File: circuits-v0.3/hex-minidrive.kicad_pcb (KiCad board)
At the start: 4 copper layers, 18 x 48 mm, 81 parts, among them X1 16MHz

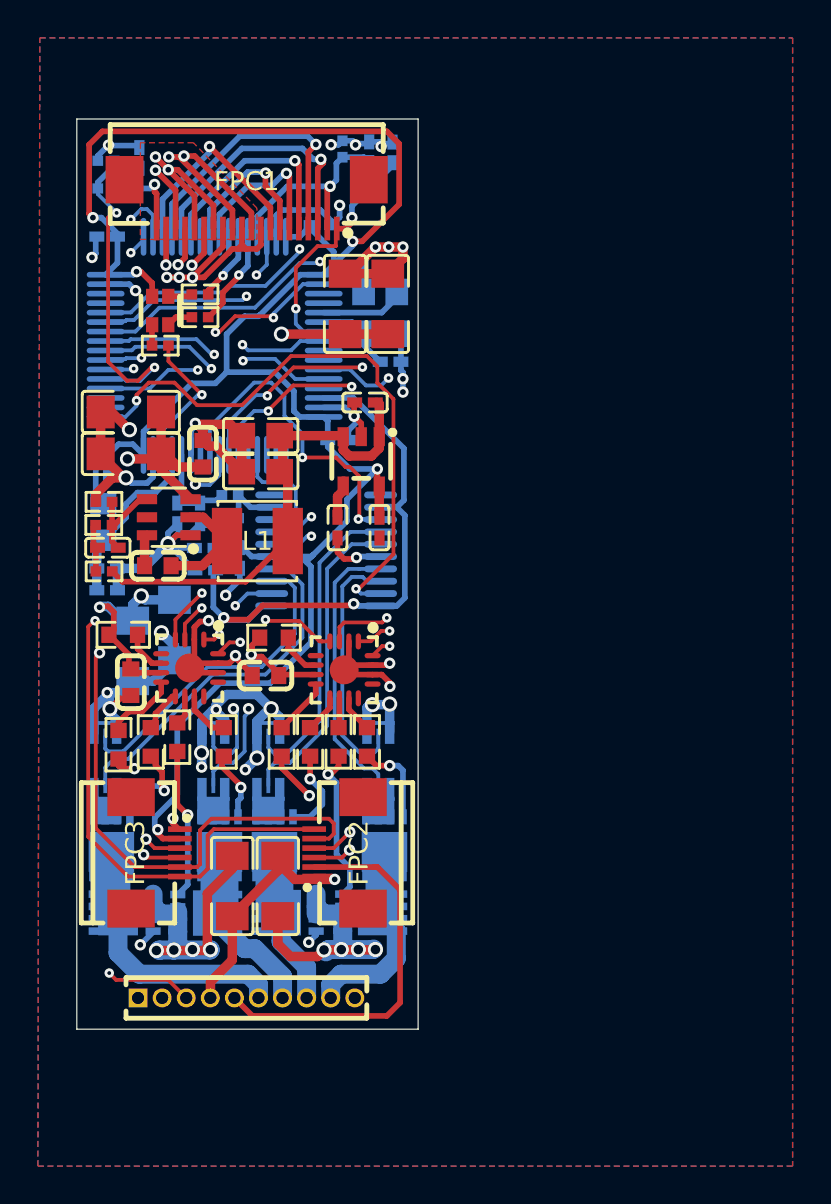
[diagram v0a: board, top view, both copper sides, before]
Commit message: Fix positioning errors and realize SPI3 is not in the bootloader options.
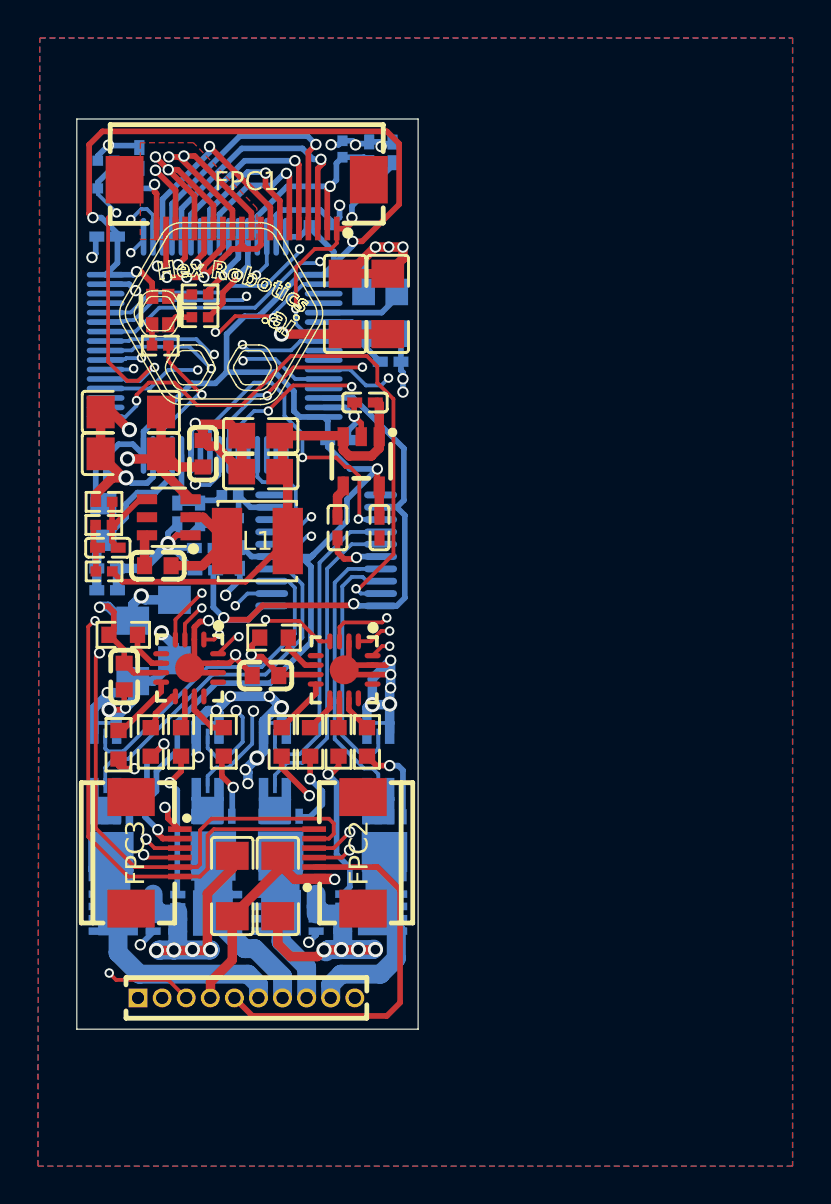
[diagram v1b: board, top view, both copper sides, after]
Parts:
- Q1, Q3, Q5, Q7: footprint Library:DFN-8_L3.0-W3.0-P0.65-BL-MOSFET -> Library:DFN-8_L3.0-W3.0-P0.65-BL-MOSFET_shifted
- moved Q3 0.96 mm to (26.2, 57.4)
- moved Q5 0.96 mm to (29.8, 57.4)
- moved Q1 0.87 mm to (20.8, 57.4)
- moved Q7 0.87 mm to (35.2, 57.4)
- moved C501 0.46 mm to (21.5, 49.4)
- moved R3 0.35 mm to (29.4, 53.9)
- moved R202 0.32 mm to (24.5, 52.9)
- moved R2 0.30 mm to (25.9, 53.9)
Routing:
- net GND: track 154.2 -> 164.6 mm, vias 42 -> 46
- net -Probe-2: track 18.5 -> 19.1 mm
- net 3V3: track 145.2 -> 145.8 mm
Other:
- board text added: "SVCLK SVDIO SCL3 SDA3 3V3 GND"
- board text added: "VCC GND VCC GND VCC GND VCC GND VCC GND VCC GND SPI3_NSS SPI3_CLK SPI3_MISO SPI3_MOSI TX RX BOOT0 RESET"
- board text removed: "GND SWCLK SVDIO 5V 3V3 POT1 POT2 POT3 TOOL DIR"
- board text removed: "IO2 IO1 I2C2_SCL I2C2_SDA 3V3 GND"
- board text removed: "IO2 IO1 I2C3_SCL I2C3_SDA 3V3 GND"

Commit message: Sigh, SPI3 cannot be used for the bootloader, move to SPI2. Finish v0.3 again.
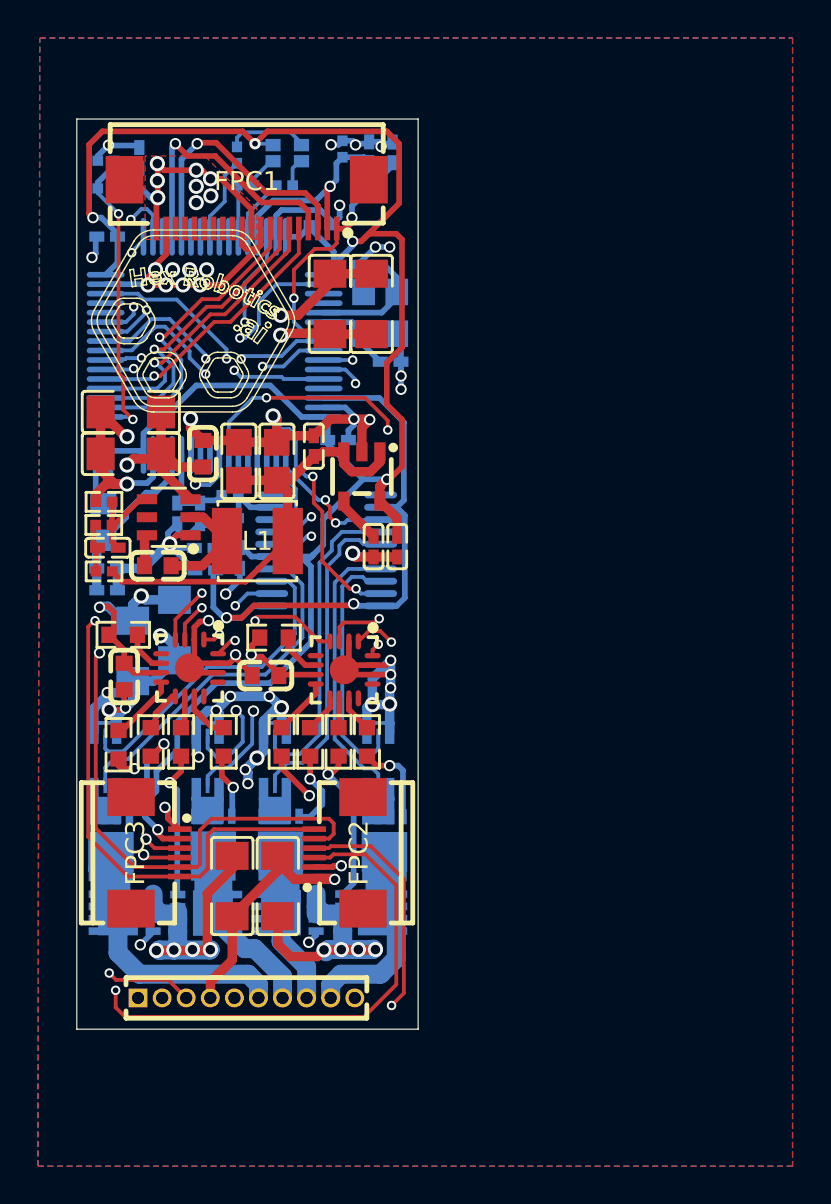
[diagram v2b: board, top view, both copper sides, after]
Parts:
- LED1, R15, R16, R17: moved to B.Cu
- moved R16 10.8 mm to (27.4, 21.9), turned to -90 degrees
- moved LED1 10.7 mm to (30.1, 21.8), turned to 180 degrees
- moved R15 8.25 mm to (29.9, 23.5), turned to 180 degrees
- moved R17 6.23 mm to (27.9, 23.5), turned to 0 degrees
- moved C31 3.55 mm to (31.5, 37.2), turned to -90 degrees
- moved C33 2.15 mm to (34.6, 42.5)
- moved C44 1.60 mm to (29.6, 38.0), turned to -90 degrees
- moved C32 1.37 mm to (35.9, 42.5)
- moved C45 1.27 mm to (27.6, 38.0), turned to -90 degrees
- moved C2 0.85 mm to (34.5, 29.8)
- moved U3 0.80 mm to (34.0, 38.9)
- moved C3 0.80 mm to (32.4, 29.8)
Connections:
- C115 pad 2: ADC2_IN15/VOLTAGE -> ADC2_IN14/VOLTAGE
- FPC1 pad 5: SPI3_MOSI -> SPI2_MOSI
- FPC1 pad 6: SPI3_MISO -> SPI2_MISO
- FPC1 pad 7: SPI3_SCK -> SPI2_SCK
- FPC1 pad 8: SPI3_NSS -> SPI2_NSS
- R16 pad 2: TIM2_CH3/BLUE_LED -> TIM2_CH2/BLUE_LED
- R18 pad 1: ADC2_IN15/VOLTAGE -> ADC2_IN14/VOLTAGE
- R19 pad 2: ADC2_IN15/VOLTAGE -> ADC2_IN14/VOLTAGE
- U1 pad 10: unconnected-(U1-PC2-Pad10) -> TIM1_CH3
- U1 pad 17: unconnected-(U1-PA3-Pad17) -> ADC1_IN4/M3_CURRENT
- U1 pad 18: unconnected-(U1-PA4-Pad18) -> ADC2_IN17/M4_CURRENT
- U1 pad 22: I2C2_SCL -> unconnected-(U1-PC4-Pad22)
- U1 pad 25: ADC1_IN12/M3_CURRENT -> unconnected-(U1-PB1-Pad25)
- U1 pad 30: TIM2_CH3/BLUE_LED -> unconnected-(U1-PB10-Pad30)
- U1 pad 33: ADC2_IN14/M4_CURRENT -> ADC2_IN14/VOLTAGE
- U1 pad 34: unconnected-(U1-PB12-Pad34) -> SPI2_NSS
- U1 pad 35: unconnected-(U1-PB13-Pad35) -> SPI2_SCK
- U1 pad 36: TIM1_CH2N -> SPI2_MISO
- U1 pad 37: ADC2_IN15/VOLTAGE -> SPI2_MOSI
- U1 pad 43: TIM1_CH2 -> I2C2_SCL
- U1 pad 44: TIM1_CH3 -> unconnected-(U1-PA10-Pad44)
- U1 pad 46: unconnected-(U1-PA12-Pad46) -> TIM1_CH2N
- U1 pad 51: SPI3_NSS -> unconnected-(U1-PA15-Pad51)
- U1 pad 54: SPI3_MOSI -> unconnected-(U1-PC12-Pad54)
- U1 pad 56: SPI3_SCK -> TIM2_CH2/BLUE_LED
- U1 pad 57: SPI3_MISO -> unconnected-(U1-PB4-Pad57)
- U1 pad 9: unconnected-(U1-PC1-Pad9) -> TIM1_CH2
- U2 pad 13: ADC1_IN12/M3_CURRENT -> ADC1_IN4/M3_CURRENT
- U2 pad 19: ADC2_IN14/M4_CURRENT -> ADC2_IN17/M4_CURRENT
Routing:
- net I2C2_SCL: track 35.8 -> 69.1 mm, vias 3 -> 2
- net ADC2_IN14/M4_CURRENT: track 31.6 -> 0.00 mm, vias 2 -> 0
- net ADC2_IN15/VOLTAGE: track 19.2 -> 0.00 mm, vias 2 -> 0
- net I2C2_SDA: track 49.3 -> 68.3 mm
- net ADC2_IN14/VOLTAGE: track 0.00 -> 17.8 mm, vias 0 -> 2
- net ADC1_IN12/M3_CURRENT: track 17.2 -> 0.00 mm, vias 2 -> 0
- net TIM1_CH3: track 36.8 -> 20.1 mm
- net SPI2_NSS: track 0.00 -> 16.3 mm, vias 0 -> 1
- net SPI2_SCK: track 0.00 -> 16.1 mm, vias 0 -> 1
- net VCC: track 90.5 -> 74.6 mm, vias 19 -> 21
- net SPI2_MISO: track 0.00 -> 15.2 mm, vias 0 -> 1
- net SPI2_MOSI: track 0.00 -> 14.2 mm, vias 0 -> 1
- net ADC2_IN17/M4_CURRENT: track 0.00 -> 13.7 mm, vias 0 -> 2
- net SPI3_MOSI: track 11.5 -> 0.00 mm, vias 1 -> 0
- net SPI3_NSS: track 11.4 -> 0.00 mm, vias 1 -> 0
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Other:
- board text added: "VCC GND ... SPI3_NSS SPI3_CLK SPI3_MISO SPI3_MOSI TX RX BOOT0 RESET"
- board text removed: "VCC GND VCC GND VCC GND VCC GND VCC GND VCC GND SPI3_NSS SPI3_CLK SPI3_MISO SPI3_MOSI TX RX BOOT0 RESET"

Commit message: Finalize v0.3 and generate production files.
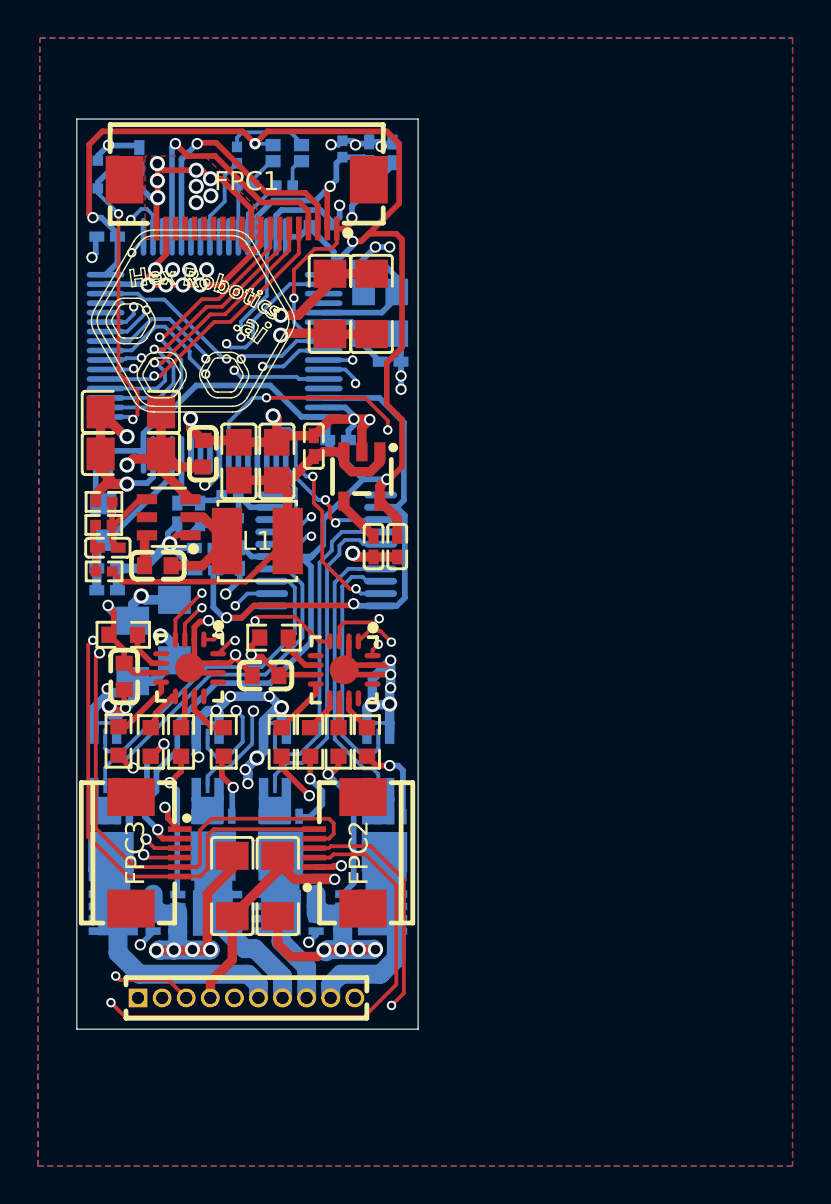
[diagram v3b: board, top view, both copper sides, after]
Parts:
- moved R102 0.20 mm to (21.2, 52.8)
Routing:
- net 3V3: track 148.5 -> 144.5 mm
- net VCC: track 74.6 -> 73.8 mm
- net TIM3_CH3/ENCODER_3: track 34.9 -> 34.1 mm
